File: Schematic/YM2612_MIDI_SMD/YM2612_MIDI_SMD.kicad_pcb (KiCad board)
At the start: 2 copper layers, 100 x 100 mm, 110 parts, among them J1 DIN-5_180, J2 TP_GND, J3 USB_B, J5 ICSP, J6 Audio-Jack-3, J7 Micro_SD_Card, SW1 Rotary_Encoder_Switch, SW10 SW_Push_Dual, SW2 SW_Push_Dual, SW3 SW_Push_Dual, SW4 SW_Push_Dual, SW5 SW_Push_Dual, SW6 SW_Push_Dual, SW7 SW_Push_Dual, SW8 SW_Push_Dual, SW9 SW_Push_Dual, U1 H11L1, U10 LD1117S50TR_SOT223, U2 AT90USB1286-AU, U3 YM2612, U4 SN76489, U5 SD6271LR, U6 LD1117S33TR_SOT223, U7 4050, U8 TL072, U9 LD1117S50TR_SOT223, Y1 16MHz

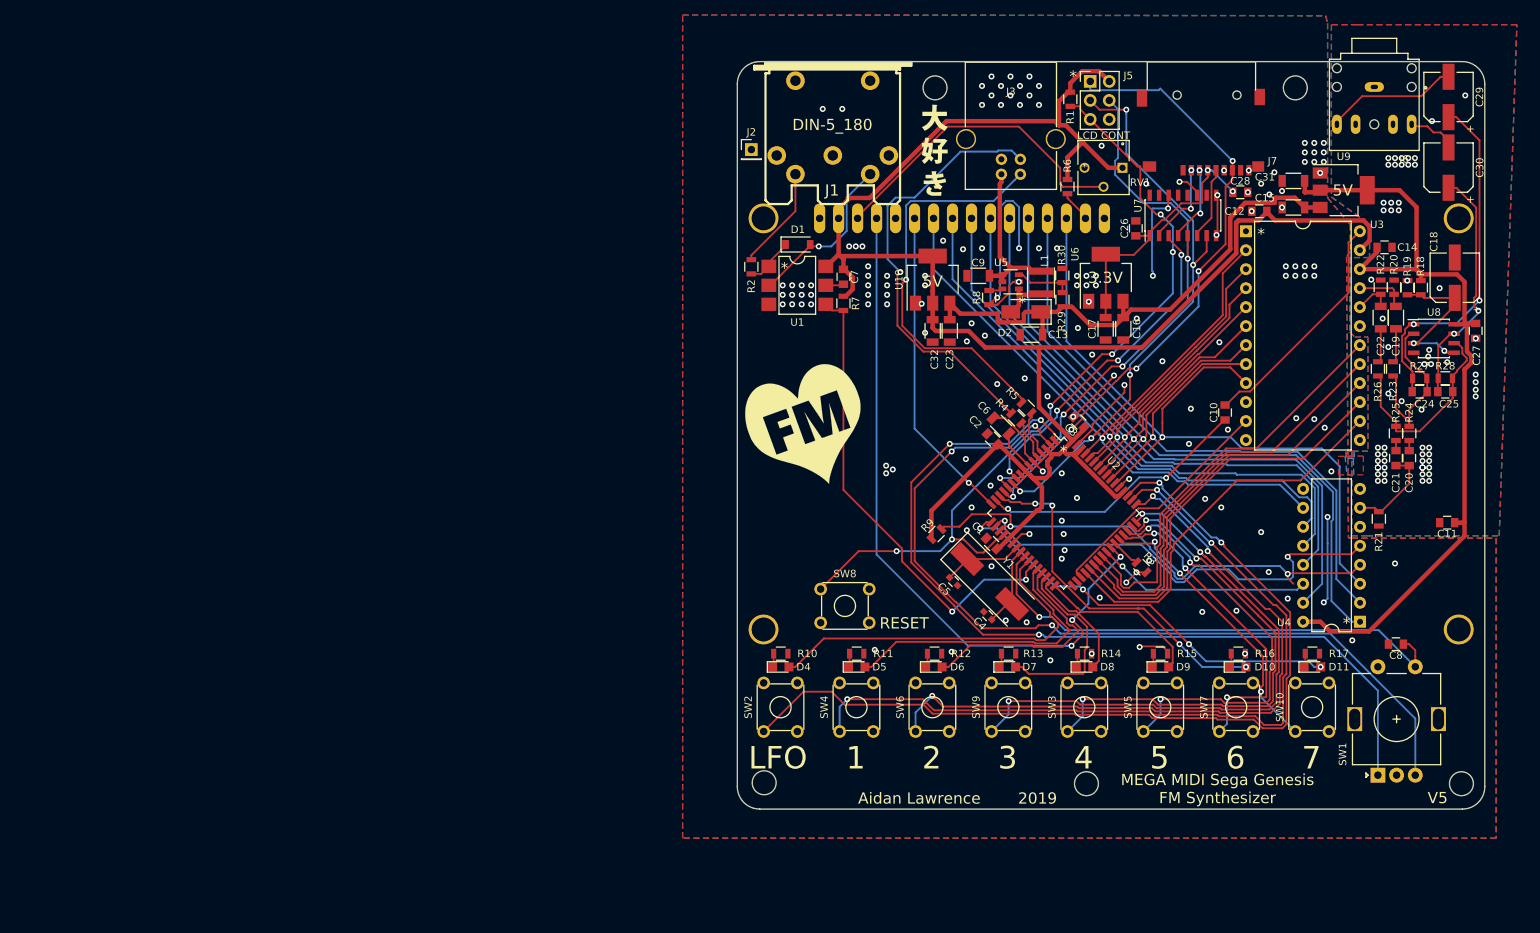
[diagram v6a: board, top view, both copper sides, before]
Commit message: New boost circuit
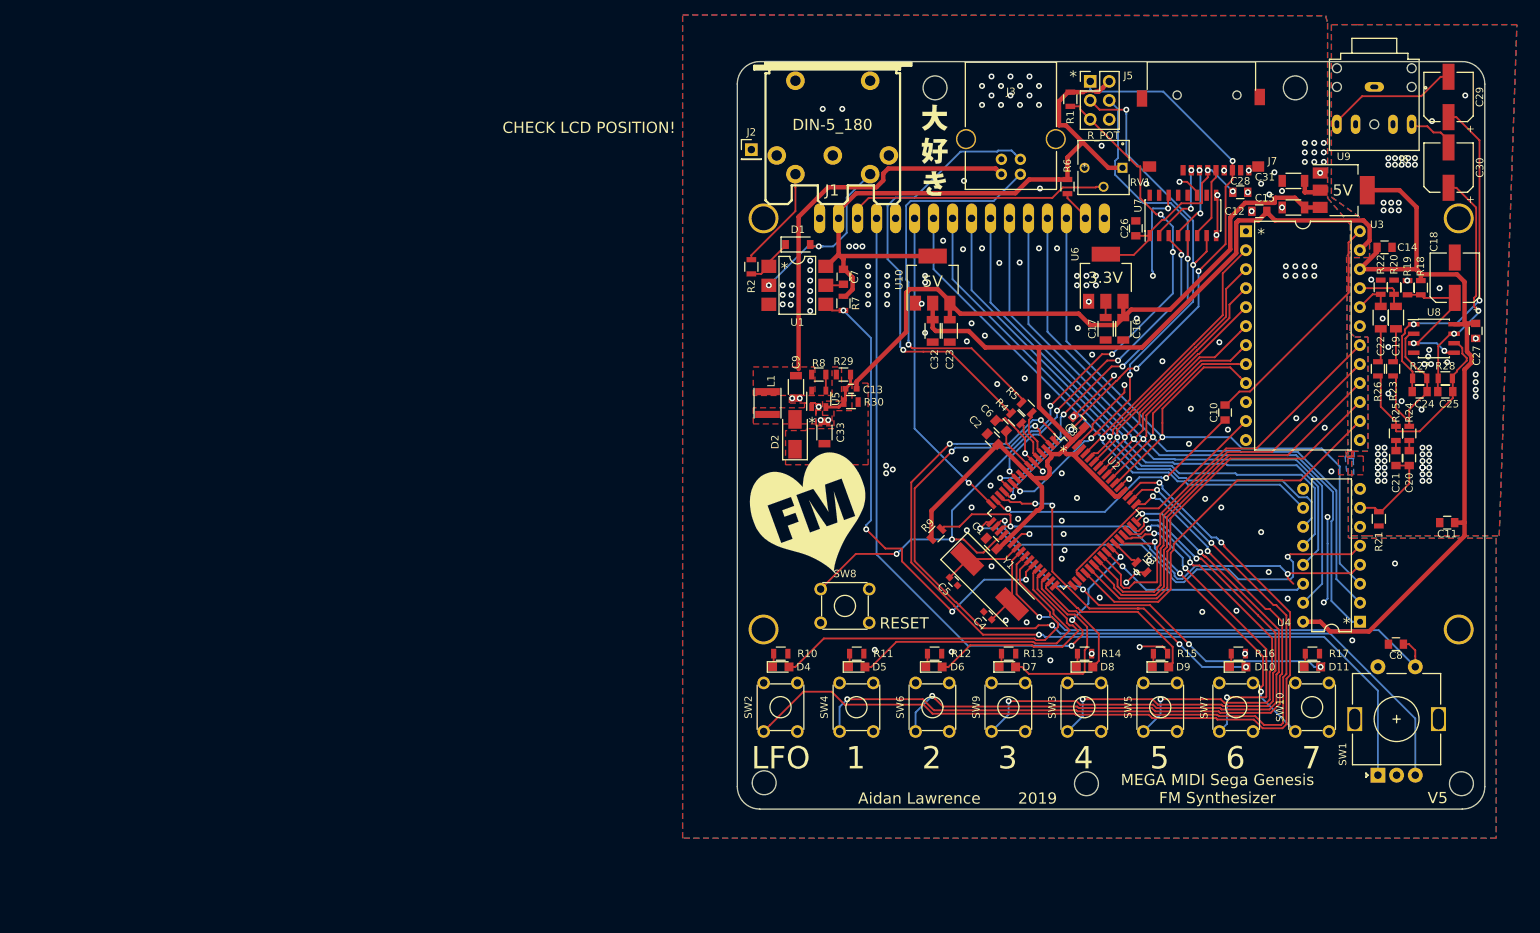
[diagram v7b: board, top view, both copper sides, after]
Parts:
- added C33: 10uF, Capacitors_SMD:C_1206, F.Cu at (184.7, 94.6)
- C13: value 10uF -> 220pF; footprint Capacitors_SMD:C_1206 -> Capacitors_SMD:C_0603
- C6: footprint Capacitors_SMD:C_1206 -> Capacitors_SMD:C_0805
- L1: value 4.7uH -> 10uH
- R21: value 2.2K -> 1.3K
- R24, R25: value 51K -> 150K
- R29: value 10K -> 12K
- R30: value 1K -> 51K
- RV1: value LCD CONT -> R_POT
- U5: value SD6271LR -> LM2733XMF; footprint TO_SOT_Packages_SMD:SOT-23-6 -> TO_SOT_Packages_SMD:SOT-23-5
- moved L1 40.0 mm to (177.0, 92.2)
- moved D2 34.9 mm to (180.7, 94.9), turned to 90 degrees
- moved R30 32.9 mm to (188.2, 90.6), turned to 180 degrees
- moved R29 31.0 mm to (187.2, 86.9), turned to 0 degrees
- moved U5 30.1 mm to (183.9, 90.1), turned to 90 degrees
- moved C9 28.6 mm to (180.8, 88.5), turned to 270 degrees
- moved C13 25.2 mm to (188.2, 88.8), turned to 180 degrees
- moved R8 25.0 mm to (183.9, 86.9), turned to 0 degrees
- moved G*** 11.8 mm to (183.3, 106.0)
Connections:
- C13 pad 1: GND -> VBOOST
- C13 pad 2: 6.6VBOOST -> Net-(C13-Pad2)
- C15 pad 2: 6.6VBOOST -> VBOOST
- C16 pad 2: 6.6VBOOST -> VBOOST
- C23 pad 2: 6.6VBOOST -> VBOOST
- C9 pad 1: GND -> VBUS
- C9 pad 2: VBUS -> GND
- D2 pad 1: 6.6VBOOST -> VBOOST
- R29 pad 1: 6.6VBOOST -> GND
- R29 pad 2: Net-(R29-Pad2) -> Net-(C13-Pad2)
- R30 pad 1: Net-(R29-Pad2) -> VBOOST
- R30 pad 2: GND -> Net-(C13-Pad2)
- R8 pad 1: Net-(R8-Pad1) -> VBUS
- R8 pad 2: GND -> Net-(R8-Pad2)
- U10 pad 3: 6.6VBOOST -> VBOOST
- U5 pad 3: Net-(R29-Pad2) -> Net-(C13-Pad2)
- U5 pad 4: VBUS -> Net-(R8-Pad2)
- U6 pad 3: 6.6VBOOST -> VBOOST
- U9 pad 3: 6.6VBOOST -> VBOOST
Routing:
- net VBOOST: track 0.00 -> 88.7 mm
- net 6.6VBOOST: track 72.2 -> 0.00 mm
- net VBUS: track 21.7 -> 51.0 mm
- net GND: track 106.1 -> 77.6 mm, vias 218 -> 226
- net +5V: track 251.0 -> 242.6 mm
- net Net-(R29-Pad2): track 7.58 -> 0.00 mm
- net Net-(C13-Pad2): track 0.00 -> 7.26 mm
- net Net-(D2-Pad2): track 6.87 -> 0.00 mm
- net +3V3: track 35.8 -> 29.5 mm
- net +5VA: track 112.7 -> 106.4 mm
- net Net-(DS1-Pad3): track 42.7 -> 36.6 mm
- net Net-(R8-Pad2): track 0.00 -> 2.15 mm
- net Net-(D1-Pad2): track 22.6 -> 24.6 mm, vias 1 -> 2
- net Net-(R8-Pad1): track 1.86 -> 0.00 mm
- net MIDI_IN: track 63.1 -> 64.9 mm, vias 2 -> 4
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- added copper zone on F.Cu, net Net-(D2-Pad2)
- added copper zone on F.Cu, net VBOOST
- added copper zone on F.Cu, net VBUS
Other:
- board text added: "CHECK LCD POSITION!"

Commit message: New boost circuit
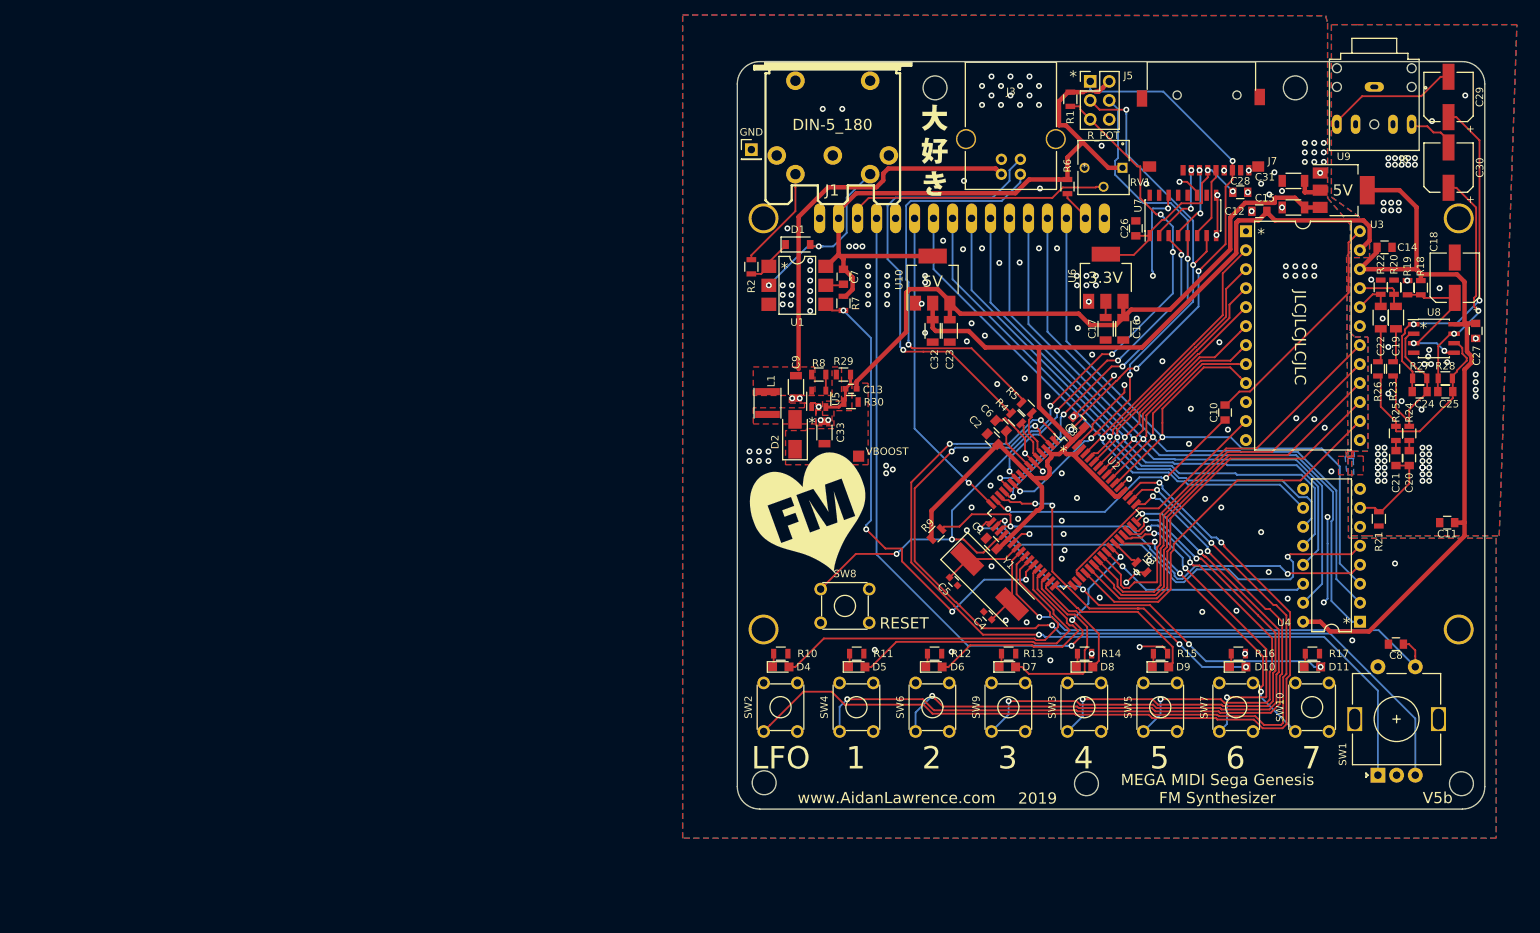
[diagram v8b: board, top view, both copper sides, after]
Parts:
- added VBOOST: Measurement_Point_Square-SMD-Pad_Small, Measurement_Points:Measurement_Point_Square-SMD-Pad_Small, F.Cu at (189.2, 97.8)
- MP1, MP2, MP3: renamed from G***; value LOGO -> GRAPHIC
- renumbered J2 to GND
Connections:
- J3 pad 5: GND -> (no net)
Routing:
- net PSG_RDY: track 66.6 -> 64.9 mm
- net USB_D-: track 54.5 -> 55.1 mm
- net GND: vias 226 -> 233
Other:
- board text added: "JLCJLCJLCJLC"
- board text added: "V5b"
- board text added: "www.AidanLawrence.com"
- board text removed: "Aidan Lawrence"
- board text removed: "CHECK LCD POSITION!"
- board text removed: "V5"
